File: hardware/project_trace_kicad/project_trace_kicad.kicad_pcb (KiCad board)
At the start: 2 copper layers, 0 parts

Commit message: PCB start
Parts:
- added C201: 3n3, Capacitor_SMD:C_0603_1608Metric_Pad1.08x0.95mm_HandSolder, F.Cu at (31.0, 14.3)
- added C202: 100n, Capacitor_SMD:C_0603_1608Metric_Pad1.08x0.95mm_HandSolder, F.Cu at (31.0, 16.8)
- added C203: 100n, Capacitor_SMD:C_0603_1608Metric_Pad1.08x0.95mm_HandSolder, F.Cu at (31.0, 19.3)
- added C204: 100n, Capacitor_SMD:C_0603_1608Metric_Pad1.08x0.95mm_HandSolder, F.Cu at (31.0, 21.8)
- added C205: 3n3, Capacitor_SMD:C_0603_1608Metric_Pad1.08x0.95mm_HandSolder, F.Cu at (31.0, 24.3)
- added C301: 100n, Capacitor_SMD:C_0603_1608Metric_Pad1.08x0.95mm_HandSolder, F.Cu at (60.4, 14.3)
- added C303: 100n, Capacitor_SMD:C_0603_1608Metric_Pad1.08x0.95mm_HandSolder, F.Cu at (60.4, 16.8)
- added C304: 10u, Capacitor_SMD:C_0805_2012Metric_Pad1.18x1.45mm_HandSolder, F.Cu at (55.9, 14.5)
- added C306: 10u, Capacitor_SMD:C_0805_2012Metric_Pad1.18x1.45mm_HandSolder, F.Cu at (55.9, 17.5)
- added C307: 100n, Capacitor_SMD:C_0603_1608Metric_Pad1.08x0.95mm_HandSolder, F.Cu at (60.4, 19.3)
- added C308: 100n, Capacitor_SMD:C_0603_1608Metric_Pad1.08x0.95mm_HandSolder, F.Cu at (60.4, 21.8)
- added C309: 100n, Capacitor_SMD:C_0603_1608Metric_Pad1.08x0.95mm_HandSolder, F.Cu at (60.4, 24.3)
- added C311: 100n, Capacitor_SMD:C_0603_1608Metric_Pad1.08x0.95mm_HandSolder, F.Cu at (60.4, 26.8)
- added C312: 100n, Capacitor_SMD:C_0603_1608Metric_Pad1.08x0.95mm_HandSolder, F.Cu at (60.4, 29.3)
- added C316: 100n, Capacitor_SMD:C_0603_1608Metric_Pad1.08x0.95mm_HandSolder, F.Cu at (64.8, 14.3)
- added C317: 100n, Capacitor_SMD:C_0603_1608Metric_Pad1.08x0.95mm_HandSolder, F.Cu at (64.8, 16.8)
- added C318: 100n, Capacitor_SMD:C_0603_1608Metric_Pad1.08x0.95mm_HandSolder, F.Cu at (64.8, 19.3)
- added C319: 100n, Capacitor_SMD:C_0603_1608Metric_Pad1.08x0.95mm_HandSolder, F.Cu at (64.8, 21.8)
- added C320: 100n, Capacitor_SMD:C_0603_1608Metric_Pad1.08x0.95mm_HandSolder, F.Cu at (64.8, 24.3)
- added C321: 100n, Capacitor_SMD:C_0603_1608Metric_Pad1.08x0.95mm_HandSolder, F.Cu at (64.8, 26.8)
- added C322: 100n, Capacitor_SMD:C_0603_1608Metric_Pad1.08x0.95mm_HandSolder, F.Cu at (64.8, 29.3)
- added C323: 10u, Capacitor_SMD:C_0805_2012Metric_Pad1.18x1.45mm_HandSolder, F.Cu at (55.9, 20.5)
- added C324: 10u, Capacitor_SMD:C_0805_2012Metric_Pad1.18x1.45mm_HandSolder, F.Cu at (55.9, 23.5)
- added C325: 10u, Capacitor_SMD:C_0805_2012Metric_Pad1.18x1.45mm_HandSolder, F.Cu at (55.9, 26.5)
- added C326: 100n, Capacitor_SMD:C_0603_1608Metric_Pad1.08x0.95mm_HandSolder, F.Cu at (69.1, 14.3)
- added C327: 10u, Capacitor_SMD:C_0805_2012Metric_Pad1.18x1.45mm_HandSolder, F.Cu at (55.9, 29.6)
- added D201: SMAJ250A, Diode_SMD:D_SMA_Handsoldering, F.Cu at (17.0, 79.5)
- added DZ201: EZA-EG3A50AV, Diode_SMD:D_0603_1608Metric_Pad1.05x0.95mm_HandSolder, F.Cu at (23.6, 92.0)
- added DZ202: EZA-EG3A50AV, Diode_SMD:D_0603_1608Metric_Pad1.05x0.95mm_HandSolder, F.Cu at (21.0, 92.0)
- added J204: Screw_Terminal_01x04, ProjectTraceFootprints:691210910004, F.Cu at (16.0, 84.4)
- added J205: Conn_Coaxial, ProjectTraceFootprints:BNC_Female_0731385003, F.Cu at (18.1, 69.5)
- added J503: Screw_Terminal_01x04, ProjectTraceFootprints:691210910004, F.Cu at (65.8, 47.2)
- added JP201: SolderJumper_2_Open, Jumper:SolderJumper-2_P1.3mm_Open_RoundedPad1.0x1.5mm, F.Cu at (43.9, 78.0)
- added JP202: SolderJumper_2_Open, Jumper:SolderJumper-2_P1.3mm_Open_RoundedPad1.0x1.5mm, F.Cu at (35.6, 125.2)
- added JP203: SolderJumper_2_Open, Jumper:SolderJumper-2_P1.3mm_Open_RoundedPad1.0x1.5mm, F.Cu at (35.6, 128.7)
- added JP204: SolderJumper_2_Open, Jumper:SolderJumper-2_P1.3mm_Open_RoundedPad1.0x1.5mm, F.Cu at (31.0, 48.0)
- added JP205: SolderJumper_2_Open, Jumper:SolderJumper-2_P1.3mm_Open_RoundedPad1.0x1.5mm, F.Cu at (31.0, 51.6)
- added JP301: SolderJumper_2_Open, Jumper:SolderJumper-2_P1.3mm_Open_RoundedPad1.0x1.5mm, F.Cu at (77.8, 14.8)
- added JP302: SolderJumper_2_Open, Jumper:SolderJumper-2_P1.3mm_Open_RoundedPad1.0x1.5mm, F.Cu at (77.8, 18.3)
- added R201: 100m, Resistor_SMD:R_2512_6332Metric_Pad1.40x3.35mm_HandSolder, F.Cu at (24.1, 87.5)
- added R202: 1M8, Resistor_SMD:R_0805_2012Metric_Pad1.20x1.40mm_HandSolder, F.Cu at (24.5, 79.5)
- added R203: 10k, Resistor_SMD:R_0603_1608Metric_Pad0.98x0.95mm_HandSolder, F.Cu at (31.0, 26.8)
- added R204: 89k8, Resistor_SMD:R_0603_1608Metric_Pad0.98x0.95mm_HandSolder, F.Cu at (31.0, 29.3)
- added R205: 180K, Resistor_SMD:R_0603_1608Metric_Pad0.98x0.95mm_HandSolder, F.Cu at (27.0, 101.5)
- added R206: 20K, Resistor_SMD:R_0603_1608Metric_Pad0.98x0.95mm_HandSolder, F.Cu at (22.0, 101.0)
- added R207: 1M8, Resistor_SMD:R_0805_2012Metric_Pad1.20x1.40mm_HandSolder, F.Cu at (48.3, 44.1)
- added R209: 620R, Resistor_THT:R_Axial_DIN0207_L6.3mm_D2.5mm_P10.16mm_Horizontal, F.Cu at (22.8, 109.8)
- added R301: 10k, Resistor_SMD:R_0603_1608Metric_Pad0.98x0.95mm_HandSolder, F.Cu at (69.1, 16.8)
- added R302: 37k, Resistor_SMD:R_0603_1608Metric_Pad0.98x0.95mm_HandSolder, F.Cu at (69.1, 19.3)
- added R303: 10k, Resistor_SMD:R_0603_1608Metric_Pad0.98x0.95mm_HandSolder, F.Cu at (69.1, 21.8)
- added R309: 37k, Resistor_SMD:R_0603_1608Metric_Pad0.98x0.95mm_HandSolder, F.Cu at (69.1, 24.3)
- added R310: 37k, Resistor_SMD:R_0603_1608Metric_Pad0.98x0.95mm_HandSolder, F.Cu at (69.1, 26.8)
- added R311: 15k, Resistor_SMD:R_0603_1608Metric_Pad0.98x0.95mm_HandSolder, F.Cu at (69.1, 29.3)
- added R312: 10k, Resistor_SMD:R_0603_1608Metric_Pad0.98x0.95mm_HandSolder, F.Cu at (73.5, 14.3)
- added R313: 249, Resistor_SMD:R_0603_1608Metric_Pad0.98x0.95mm_HandSolder, F.Cu at (73.5, 16.8)
- added R314: 10k, Resistor_SMD:R_0603_1608Metric_Pad0.98x0.95mm_HandSolder, F.Cu at (73.5, 19.3)
- added R315: 15k, Resistor_SMD:R_0603_1608Metric_Pad0.98x0.95mm_HandSolder, F.Cu at (73.5, 21.8)
- added R316: 10k, Resistor_SMD:R_0603_1608Metric_Pad0.98x0.95mm_HandSolder, F.Cu at (73.5, 24.3)
- added TP201: TestPoint, TestPoint:TestPoint_Pad_1.5x1.5mm, F.Cu at (47.2, 14.8)
- added TP202: TestPoint, TestPoint:TestPoint_Pad_1.5x1.5mm, F.Cu at (35.2, 132.3)
- added TP203: TestPoint, TestPoint:TestPoint_Pad_1.5x1.5mm, F.Cu at (47.2, 21.9)
- added TP204: TestPoint, TestPoint:TestPoint_Pad_1.5x1.5mm, F.Cu at (47.2, 25.4)
- added TP206: TestPoint, TestPoint:TestPoint_Pad_1.5x1.5mm, F.Cu at (47.2, 29.0)
- added TP301: TestPoint, TestPoint:TestPoint_Pad_1.5x1.5mm, F.Cu at (77.4, 21.9)
- added U202: AQW280SX, ProjectTraceFootprints:AQW282SX, F.Cu at (34.8, 81.8)
- added U203: AQW282SX, ProjectTraceFootprints:AQW282SX, F.Cu at (27.2, 128.7)
- added U206: TLE2426xLP, Package_TO_SOT_THT:TO-92_Inline_Wide, F.Cu at (44.8, 51.7)
- added U301: LM358, Package_SO:MSOP-8_3x3mm_P0.65mm, F.Cu at (77.3, 32.9)
- added U304: MCP6499T, ProjectTraceFootprints:SOIC-14_3.9x8.7mm_P1.27mm_Handsolder, F.Cu at (62.7, 35.8)
- added U306: LM4040DBZ-2.5, Package_TO_SOT_SMD:SOT-23_Handsoldering, F.Cu at (70.3, 33.1)
- added U307: LM4040DBZ-4.1, Package_TO_SOT_SMD:SOT-23_Handsoldering, F.Cu at (70.3, 37.8)
- added U501: UA78M33QDCYRQ1, Package_TO_SOT_SMD:SOT-223-3_TabPin2, F.Cu at (58.4, 47.1)
- added U502: UA78M05QDCYRQ1, Package_TO_SOT_SMD:SOT-223-3_TabPin2, F.Cu at (58.4, 55.5)

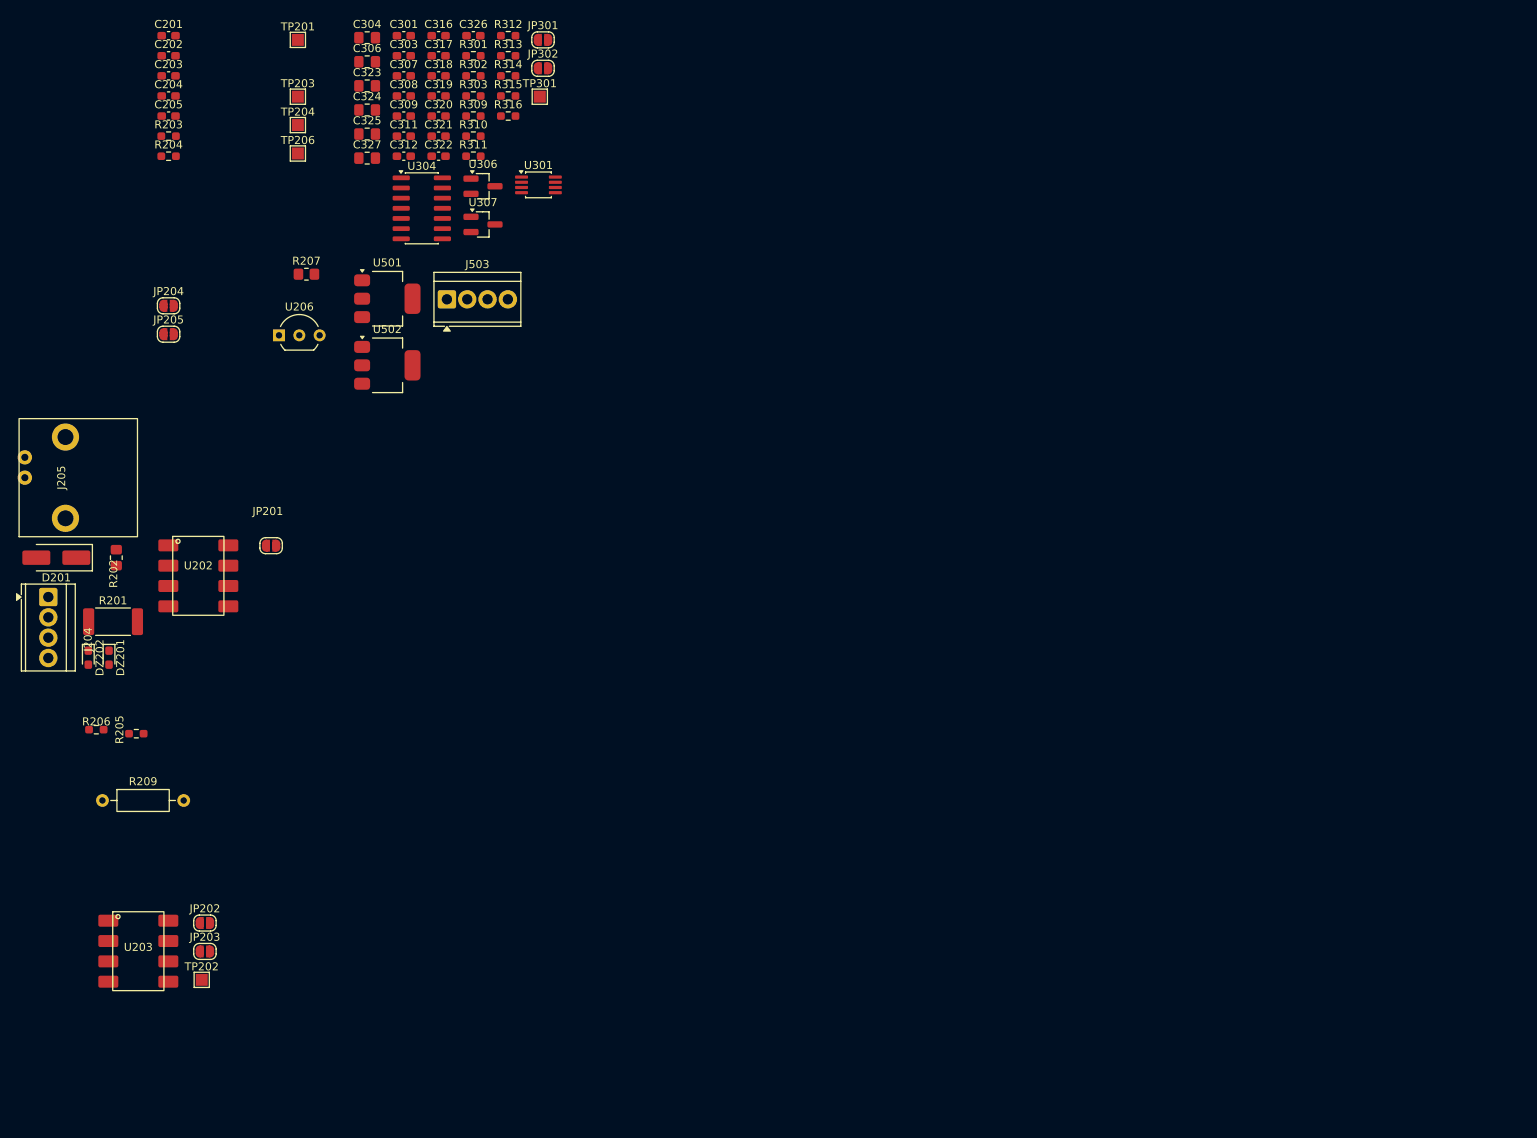
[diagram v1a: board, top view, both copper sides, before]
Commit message: Fix Footprints, Add ADC Footpring, begin Layout
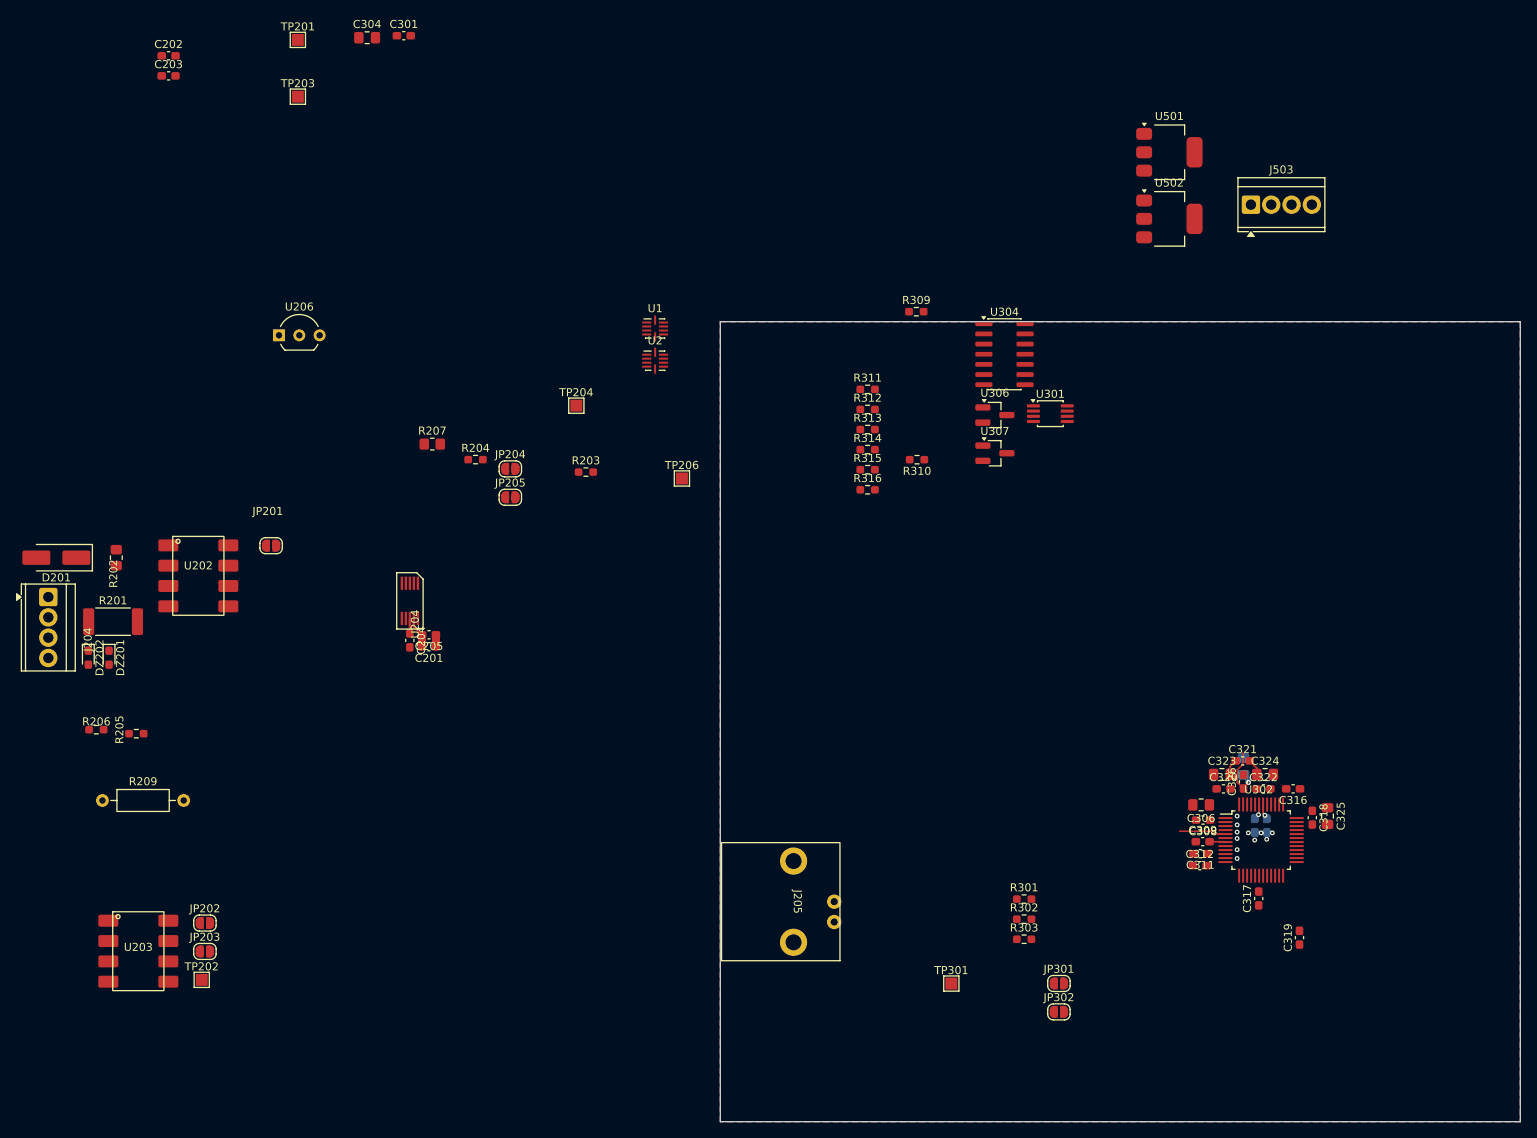
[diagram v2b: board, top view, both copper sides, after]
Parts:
- added U1: OPA2837IRUNT, ProjectTraceFootprints:OPA2837IRUNT-Handsolder, F.Cu at (91.8, 50.9)
- added U2: OPA2837IRUNT, ProjectTraceFootprints:OPA2837IRUNT-Handsolder, F.Cu at (91.8, 54.9)
- added U204: TS5A23159DGS, ProjectTraceFootprints:SOIC-10 - DGS0010A, F.Cu at (61.2, 84.9)
- added U302: ADS1602, ProjectTraceFootprints:LQFP-48_7x7_Pitch0.5mm - PFB0048A, F.Cu at (167.6, 114.8)
- C303, C307, C327: moved to B.Cu
- moved C319 150.5 mm to (172.4, 127.0), turned to 90 degrees
- moved C325 147.2 mm to (175.9, 111.8), turned to -90 degrees
- moved C317 147.0 mm to (167.3, 122.1), turned to 90 degrees
- moved C303 143.4 mm to (166.8, 113.0), turned to 90 degrees
- moved C318 143.3 mm to (174.0, 112.0), turned to -90 degrees
- moved C307 142.9 mm to (168.3, 113.0), turned to -90 degrees
- moved C316 142.4 mm to (171.6, 108.4), turned to 180 degrees
- moved C324 139.6 mm to (168.1, 106.6)
- moved C306 139.6 mm to (160.1, 110.4), turned to 180 degrees
- moved C323 137.2 mm to (162.7, 106.6)
- moved C309 134.9 mm to (160.3, 115.0)
- moved C308 134.8 mm to (160.3, 112.3), turned to 180 degrees
- moved JP302 134.4 mm to (142.3, 136.3)
- moved JP301 134.4 mm to (142.3, 132.7)
- moved C326 134.0 mm to (165.4, 107.5), turned to 90 degrees
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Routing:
- net +2V5: track 0.00 -> 7.29 mm, vias 0 -> 1
- net /ADC/Signal.In: track 0.00 -> 5.89 mm
- net +5V: track 0.00 -> 5.33 mm, vias 0 -> 1
- net Net-(JP205-A): track 0.00 -> 3.95 mm
- net +1V0: track 0.00 -> 2.30 mm
- net +4V: track 0.00 -> 2.08 mm
- net Net-(U302B-VCAP): track 0.00 -> 2.02 mm, vias 0 -> 1
- net /Inputs/AttenBuffer: track 0.00 -> 1.49 mm
- net GND: vias 0 -> 11
- added copper zone on B.Cu, net GND
- added copper zone on F.Cu, net GND
- added copper zone on In1.Cu, net GND
- added copper zone on In2.Cu, net GND
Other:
- board outline added: 100 x 100 mm
- copper layers 2 -> 4

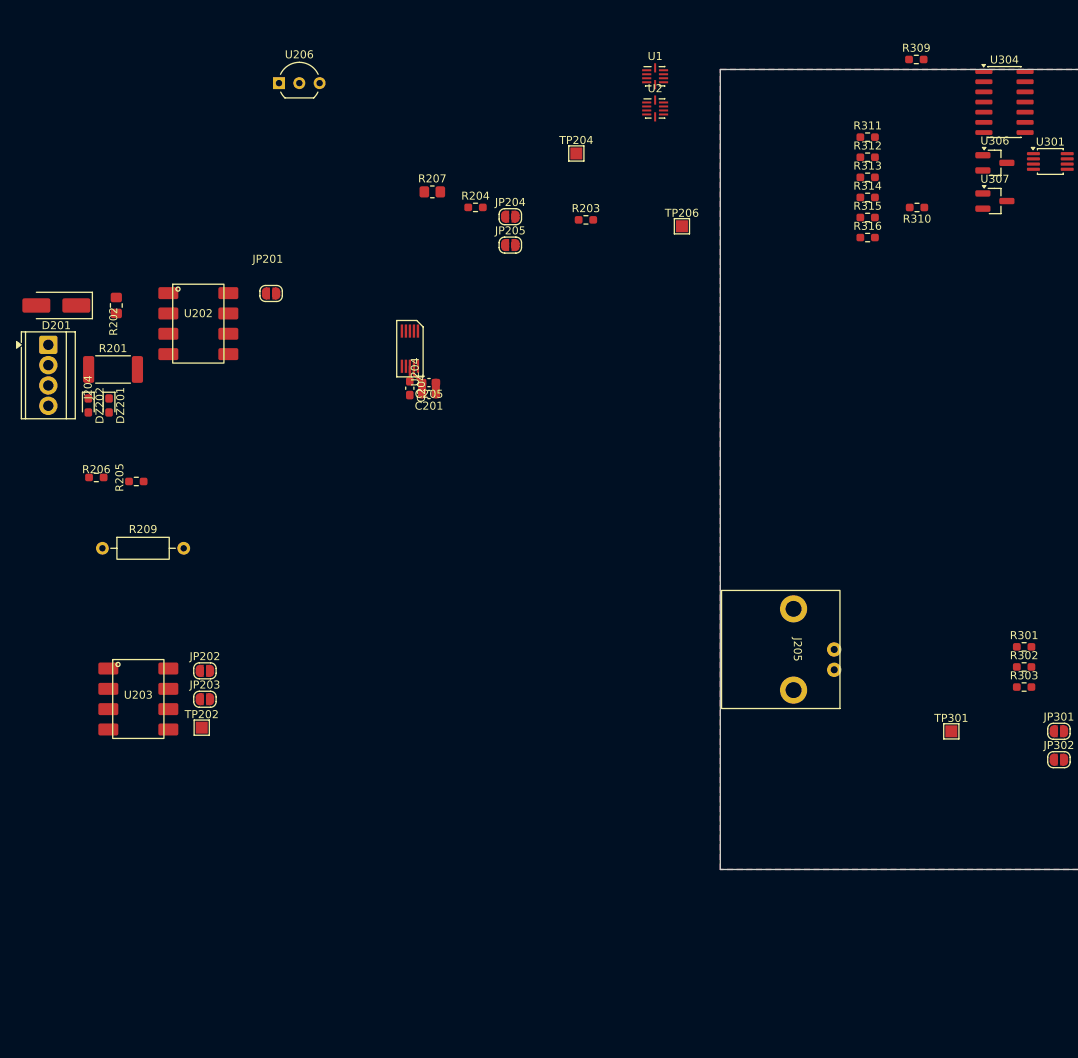
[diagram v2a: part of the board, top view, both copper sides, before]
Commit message: Skitse til første halvdel af trancing to input
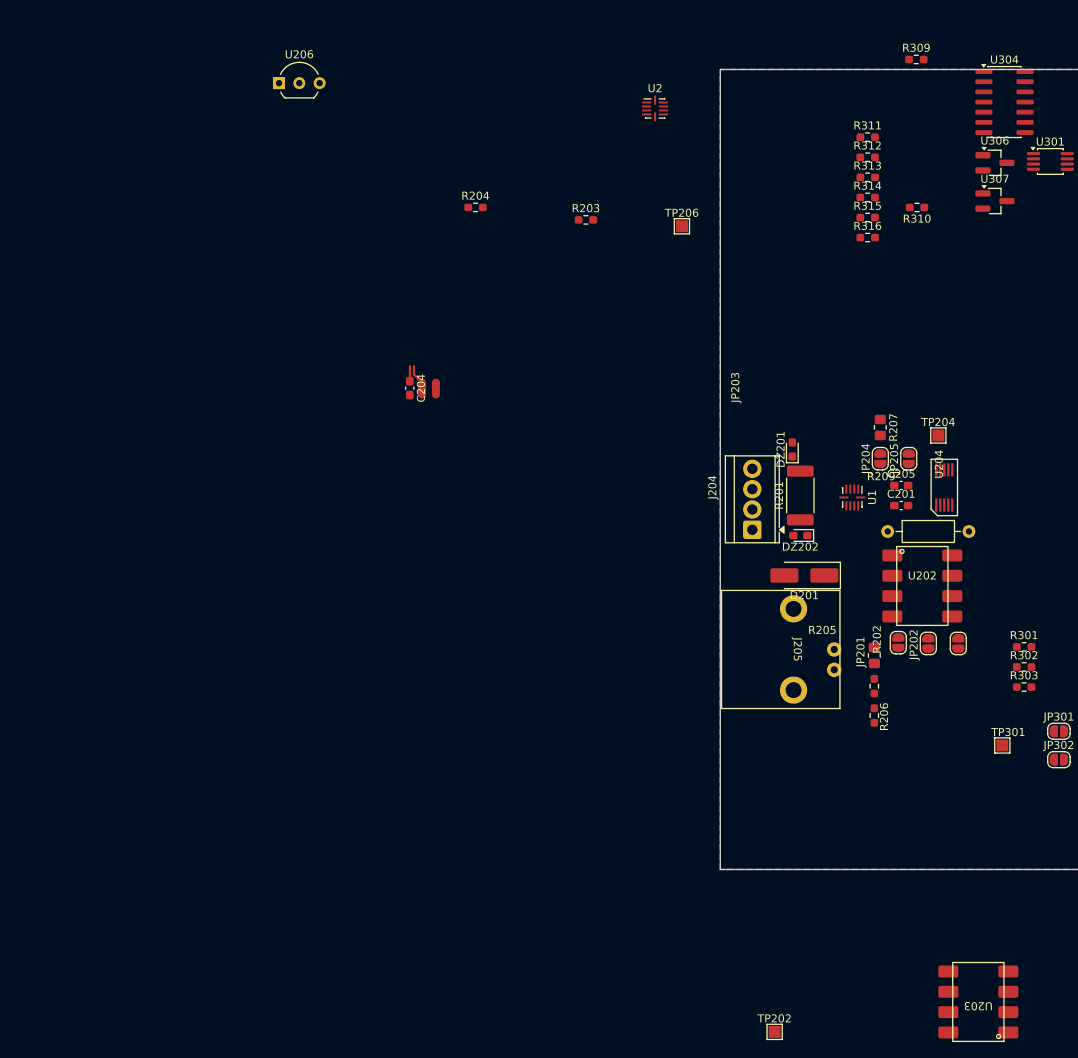
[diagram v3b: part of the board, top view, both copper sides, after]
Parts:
- moved U203 111.6 mm to (132.2, 166.6), turned to 180 degrees
- moved R202 104.4 mm to (119.2, 123.2), turned to 90 degrees
- moved R206 101.7 mm to (119.2, 130.8), turned to -90 degrees
- moved D201 99.4 mm to (110.5, 113.2)
- moved R209 98.2 mm to (120.9, 107.8)
- moved U202 96.3 mm to (125.2, 114.6)
- moved R205 95.7 mm to (119.2, 127.1), turned to -90 degrees
- moved JP203 94.4 mm to (129.8, 121.8), turned to 90 degrees
- moved J204 91.0 mm to (104.0, 107.5), turned to 90 degrees
- moved JP202 90.5 mm to (126.0, 121.8), turned to 90 degrees
- moved DZ202 90.5 mm to (110.0, 108.2), turned to 180 degrees
- moved JP201 89.7 mm to (122.2, 121.7), turned to 90 degrees
- moved R201 87.3 mm to (110.0, 103.2), turned to 90 degrees
- moved DZ201 85.6 mm to (109.0, 97.5), turned to 90 degrees
- moved TP202 81.1 mm to (106.8, 170.3)
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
